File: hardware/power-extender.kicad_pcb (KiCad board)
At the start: 2 copper layers, 90 x 71 mm, 74 parts, among them J1 IFACE RPI, J11 LOAD, J2 IFACE PASS, J21 LOAD, J3 AUX ANALOG, J31 LOAD, J4 AUX DIGITAL, J41 LOAD, K11 SRD-05VDC-SL-C, K21 SRD-05VDC-SL-C, K31 SRD-05VDC-SL-C, K41 SRD-05VDC-SL-C, Q1 BSS138, Q11 PMBT3904, Q2 BSS138, Q21 PMBT3904, Q31 PMBT3904, Q41 PMBT3904, U1 ADS1115IDGS, U11 PC817X2CSP9F, U12 CC6902SO-10A, U2 PCA9557PW, U21 PC817X2CSP9F, U22 CC6902SO-10A, U3 ADS1115IDGS, U31 PC817X2CSP9F, U32 CC6902SO-10A, U41 PC817X2CSP9F, U42 CC6902SO-10A

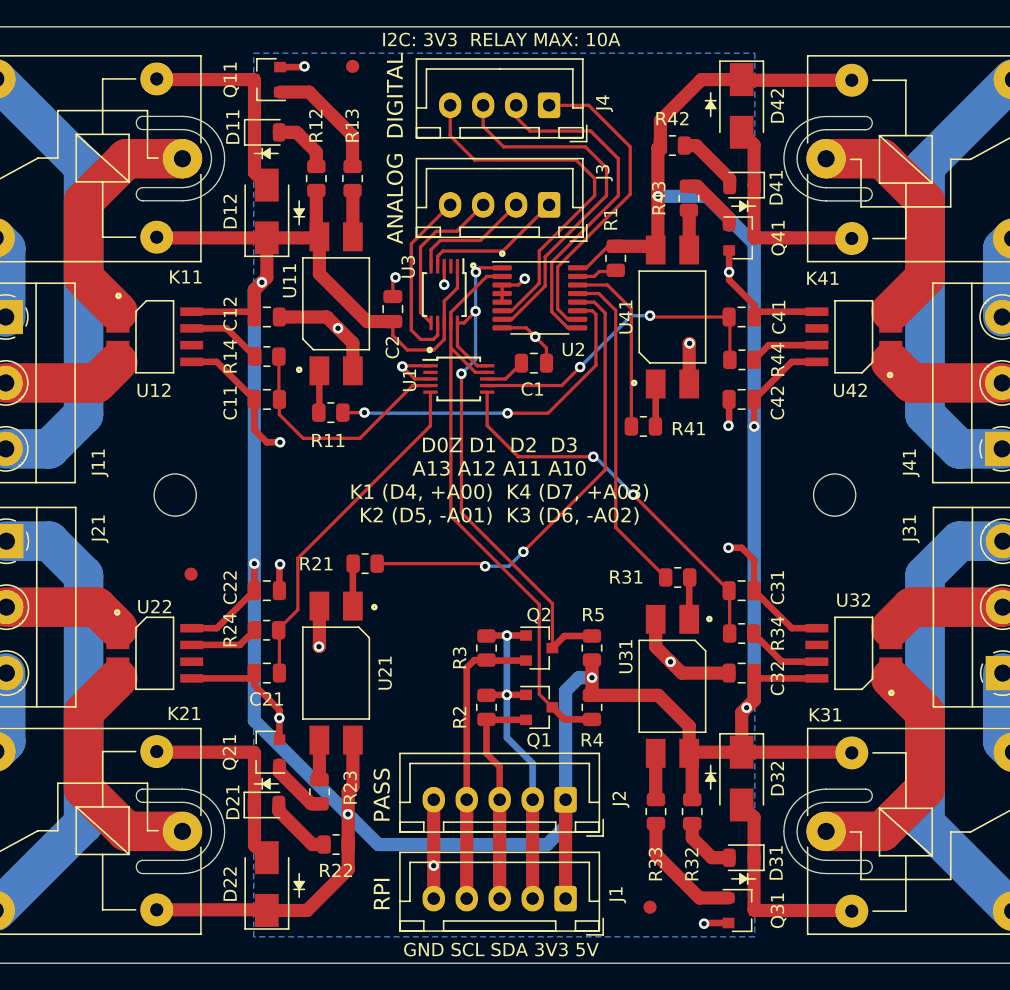
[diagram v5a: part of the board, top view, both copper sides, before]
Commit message: Add bjt pulldown, prepare for export
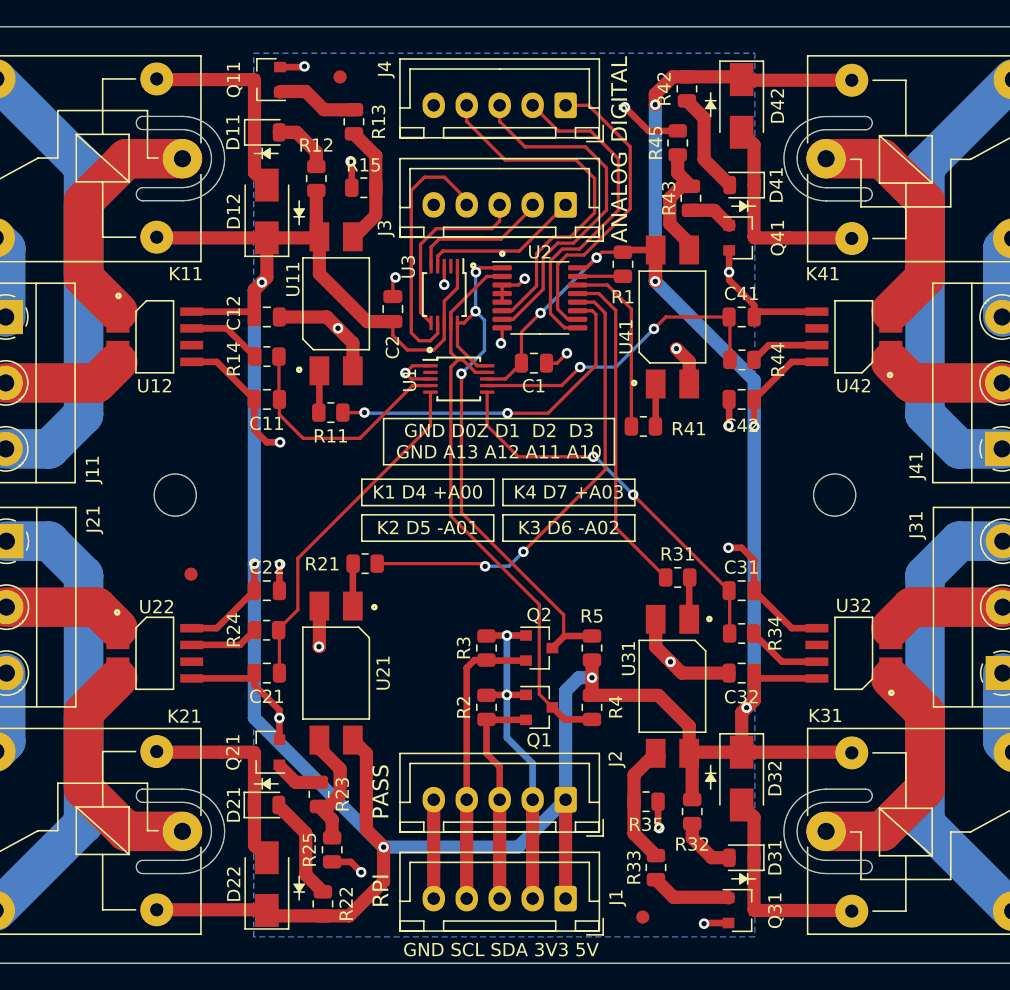
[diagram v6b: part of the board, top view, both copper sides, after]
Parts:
- added R15: 10K, Resistor_SMD:R_0805_2012Metric, F.Cu at (138.1, 77.2)
- added R25: 10K, Resistor_SMD:R_0805_2012Metric, F.Cu at (135.7, 127.4)
- added R35: 10K, Resistor_SMD:R_0805_2012Metric, F.Cu at (159.5, 123.8)
- added R45: 10K, Resistor_SMD:R_0805_2012Metric, F.Cu at (161.9, 73.8)
- J3, J4: footprint Connector_JST:JST_XH_B4B-XH-A_1x04_P2.50mm_Vertical -> Connector_JST:JST_XH_B5B-XH-A_1x05_P2.50mm_Vertical
- moved R22 4.61 mm to (135.0, 131.5), turned to 90 degrees
- moved R42 4.44 mm to (162.6, 69.7), turned to 270 degrees
- moved R13 4.30 mm to (137.3, 72.2)
- moved R33 4.25 mm to (160.2, 128.8)
- moved J3 1.25 mm to (153.4, 78.5)
- moved J4 1.25 mm to (153.4, 71.0)
- moved FID1 1.24 mm to (136.3, 68.8)
- moved FID3 0.93 mm to (159.2, 132.5)
- moved R1 0.71 mm to (157.8, 83.0)
- moved R23 0.21 mm to (134.7, 123.2), turned to 90 degrees
- moved R43 0.15 mm to (162.9, 78.0), turned to 270 degrees
- turned U11 to 90 degrees
- turned U12 to 0 degrees
- turned U21 to 270 degrees
- turned U22 to 0 degrees
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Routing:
- net +5V: track 292.8 -> 304.3 mm, vias 7 -> 10
- net GND: track 97.1 -> 105.9 mm, vias 18 -> 22
- net Net-(R23-Pad1): track 3.02 -> 9.30 mm
- net Net-(R43-Pad1): track 3.02 -> 9.30 mm
- net Net-(R33-Pad1): track 3.52 -> 9.51 mm
- net A3: track 14.1 -> 19.8 mm
- net Net-(R13-Pad1): track 3.52 -> 9.13 mm
- net Net-(Q31-Pad1): track 9.20 -> 6.07 mm
- net Net-(Q11-Pad1): track 9.20 -> 6.20 mm
- net Net-(D41-Pad2): track 4.94 -> 7.73 mm
- net Net-(D21-Pad2): track 4.94 -> 7.73 mm
- net A2: track 12.2 -> 14.2 mm
- net A1: track 9.11 -> 10.6 mm
- net SCL5V: track 43.7 -> 44.9 mm
- net A0: track 10.8 -> 12.1 mm
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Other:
- rule trace_min: 0.2 -> 0.15
- rule via_min_size: 0.4 -> 0.3
- board text added: "GND D0Z D1 D2 D3 GND A13 A12 A11 A10"
- board text added: "K1 D4 +A00"
- board text added: "K2 D5 -A01"
- board text added: "K3 D6 -A02"
- board text added: "K4 D7 +A03"
- board text removed: "D0Z D1 D2 D3 A13 A12 A11 A10 K1 (D4, +A00) K4 (D7, +A03) K2 (D5, -A01) K3 (D6, -A02)"
- board text removed: "I2C: 3V3 RELAY MAX: 10A"

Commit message: rev1 final touchups
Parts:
- D12, D22, D32, D42: footprint Diode_SMD:D_SMA -> CustomComponents:D_SMAF
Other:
- outline, holes or cut-outs redrawn
